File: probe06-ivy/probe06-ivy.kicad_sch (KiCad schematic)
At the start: 39 parts, among them SW1 SW_Push, U1 STM32F407VGTx, Y1 8 MHz, Y2 32.768 KHz

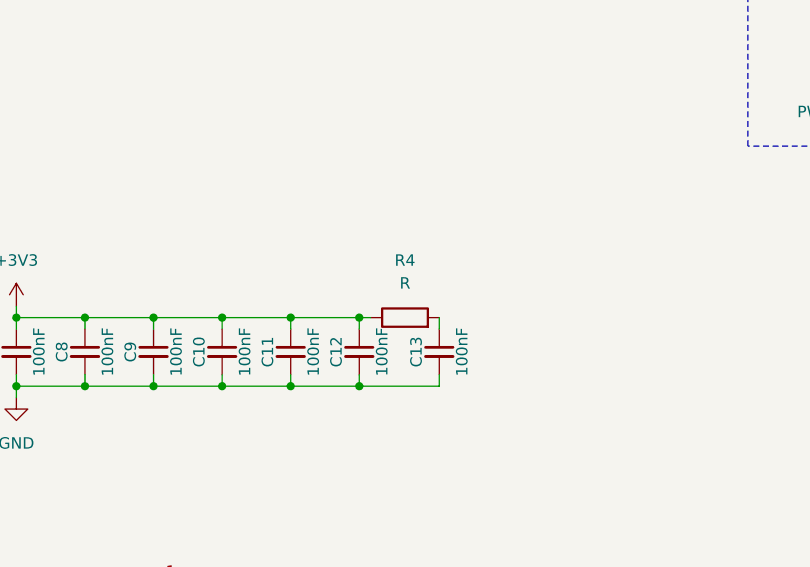
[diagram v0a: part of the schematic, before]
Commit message: Some revision to meet pcb service requirements - Change via hole diameter - Via and component placement - etc
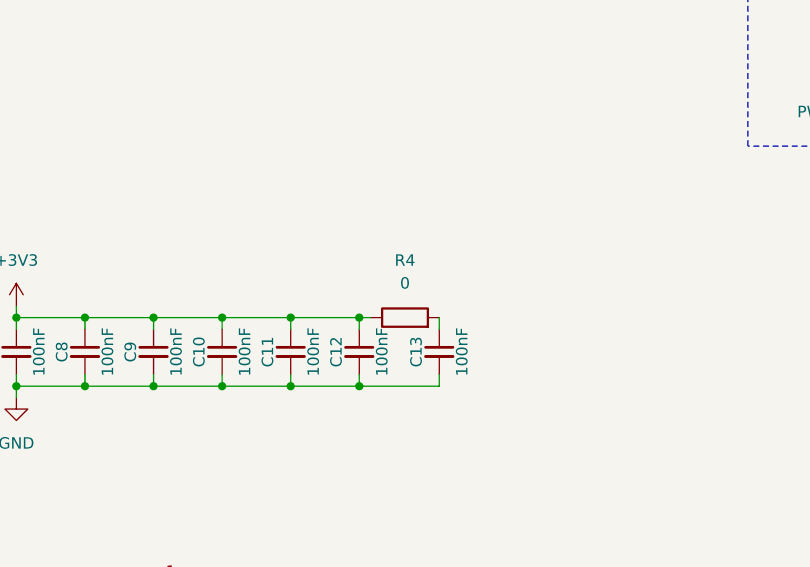
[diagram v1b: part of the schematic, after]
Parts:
- R4: value R -> 0; footprint (none) -> Resistor_SMD:R_0603_1608Metric
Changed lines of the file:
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@@
 			)
 		)
-		(property "Value" "R"
+		(property "Value" "0"
 			(at 207.01 62.23 90)
 			(effects
@@
 			)
 		)
-		(property "Footprint" ""
+		(property "Footprint" "Resistor_SMD:R_0603_1608Metric"
 			(at 207.01 67.818 90)
 			(effects

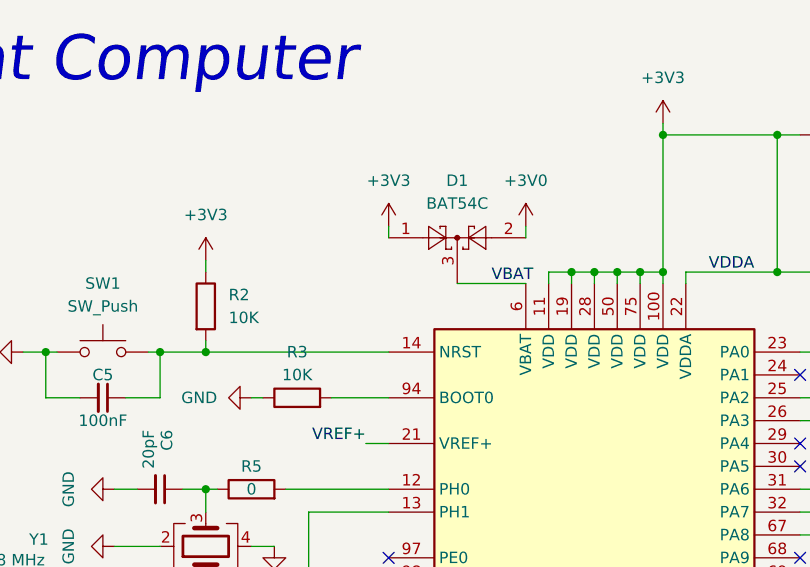
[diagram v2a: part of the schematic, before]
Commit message: rev 1.2.1 add additional pin
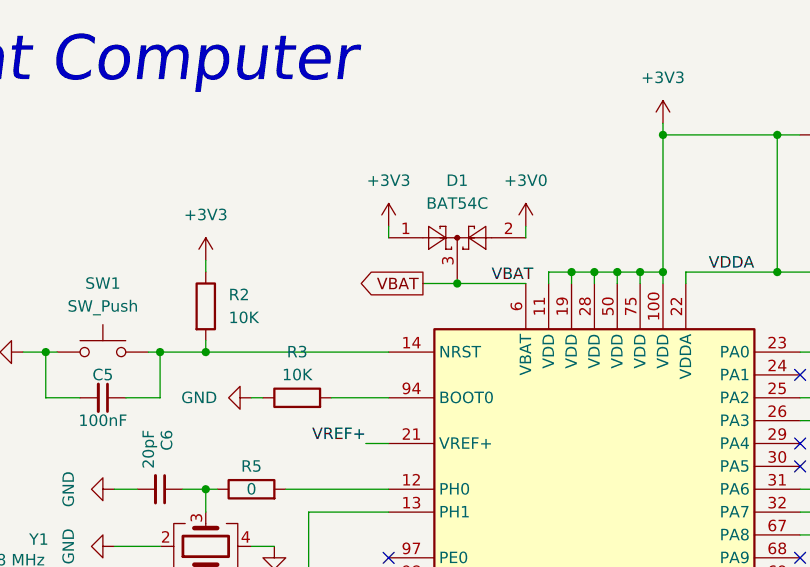
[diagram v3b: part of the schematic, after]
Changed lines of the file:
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@@
+	)
+	(junction
+		(at 82.55 44.45)
+		(diameter 0)
+		(color 0 0 0 0)
 	)
 	(junction
@@
 		(pts
 			(xy 186.69 67.31) (xy 186.69 66.04)
+		)
+		(stroke
+			(width 0)
+			(type default)
+		)
+	)
+	(wire
+		(pts
+			(xy 82.55 44.45) (xy 78.74 44.45)
 		)
 		(stroke
@@
 				(hide yes)
 			)
+		)
+	)
+	(global_label "VBAT"
+		(shape output)
+		(at 78.74 44.45 180)
+		(fields_autoplaced yes)
+		(effects
+			(font
+				(size 1.27 1.27)
+			)
+			(justify right)
+		)
+		(property "Intersheetrefs" "${INTERSHEET_REFS}"
+			(at 71.34 44.45 0)
+			(effects
+				(font
+					(size 1.27 1.27)
+				)
+				(justify right)
+				(hide yes)
+			)
